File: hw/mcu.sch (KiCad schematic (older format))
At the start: 10 parts, among them U3 MSP430G2553IPW28

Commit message: epd-clock: hw v0.2
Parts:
- added R6, R7: 4.7K, Resistor_SMD:R_0603_1608Metric, symbol Device:R
- renumbered R8 to R5
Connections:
- net +3V3: now also R6.1, R7.1
- net SCL: now also R7.2
- net SDA: now also R6.2
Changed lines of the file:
@@
 $EndDescr
 $Comp
-L power:+3V3 #PWR035
+L power:+3V3 #PWR036
 U 1 1 6113EAC6
 P 5900 2650
-F 0 "#PWR035" H 5900 2500 50  0001 C CNN
+F 0 "#PWR036" H 5900 2500 50  0001 C CNN
 F 1 "+3V3" H 5915 2823 50  0000 C CNN
 F 2 "" H 5900 2650 50  0001 C CNN
@@
 $EndComp
 $Comp
-L power:GND #PWR036
+L power:GND #PWR037
 U 1 1 6113F28C
 P 5900 4850
-F 0 "#PWR036" H 5900 4600 50  0001 C CNN
+F 0 "#PWR037" H 5900 4600 50  0001 C CNN
 F 1 "GND" H 5905 4677 50  0000 C CNN
 F 2 "" H 5900 4850 50  0001 C CNN
@@
 $EndComp
 $Comp
-L Device:R R8
+L Device:R R5
 U 1 1 6113FE92
 P 4150 2650
-F 0 "R8" H 4220 2696 50  0000 L CNN
+F 0 "R5" H 4220 2696 50  0000 L CNN
 F 1 "47K" H 4220 2605 50  0000 L CNN
 F 2 "Resistor_SMD:R_0603_1608Metric" V 4080 2650 50  0001 C CNN
@@
 	4150 2900 4150 3000
 $Comp
-L power:GND #PWR032
+L power:GND #PWR033
 U 1 1 61141837
 P 4150 3300
-F 0 "#PWR032" H 4150 3050 50  0001 C CNN
+F 0 "#PWR033" H 4150 3050 50  0001 C CNN
 F 1 "GND" H 4155 3127 50  0000 C CNN
 F 2 "" H 4150 3300 50  0001 C CNN
@@
 $EndComp
 $Comp
-L power:+3V3 #PWR031
+L power:+3V3 #PWR032
 U 1 1 61141D49
 P 4150 2500
-F 0 "#PWR031" H 4150 2350 50  0001 C CNN
+F 0 "#PWR032" H 4150 2350 50  0001 C CNN
 F 1 "+3V3" H 4165 2673 50  0000 C CNN
 F 2 "" H 4150 2500 50  0001 C CNN
@@
 $EndComp
 $Comp
-L power:+3V3 #PWR033
+L power:+3V3 #PWR034
 U 1 1 611466AB
 P 5150 1750
-F 0 "#PWR033" H 5150 1600 50  0001 C CNN
+F 0 "#PWR034" H 5150 1600 50  0001 C CNN
 F 1 "+3V3" V 5165 1878 50  0000 L CNN
 F 2 "" H 5150 1750 50  0001 C CNN
@@
 $EndComp
 $Comp
-L power:GND #PWR034
+L power:GND #PWR035
 U 1 1 61146C9B
 P 5150 1850
-F 0 "#PWR034" H 5150 1600 50  0001 C CNN
+F 0 "#PWR035" H 5150 1600 50  0001 C CNN
 F 1 "GND" V 5155 1722 50  0000 R CNN
 F 2 "" H 5150 1850 50  0001 C CNN
@@
 Text HLabel 4500 4050 0    50   Output ~ 0
 CLK
-Text HLabel 7300 3650 2    50   Output ~ 0
+Text HLabel 8350 3650 2    50   Output ~ 0
 SCL
-Text HLabel 7300 3750 2    50   BiDi ~ 0
+Text HLabel 8350 3750 2    50   BiDi ~ 0
 SDA
 Text HLabel 4500 4550 0    50   Output ~ 0
@@
 $EndComp
 $Comp
-L power:+3V3 #PWR038
+L power:+3V3 #PWR039
 U 1 1 610AD35D
 P 6450 1900
-F 0 "#PWR038" H 6450 1750 50  0001 C CNN
+F 0 "#PWR039" H 6450 1750 50  0001 C CNN
 F 1 "+3V3" V 6465 2028 50  0000 L CNN
 F 2 "" H 6450 1900 50  0001 C CNN
@@
 $EndComp
 $Comp
-L power:GND #PWR037
+L power:GND #PWR038
 U 1 1 610AD870
 P 6150 1900
-F 0 "#PWR037" H 6150 1650 50  0001 C CNN
+F 0 "#PWR038" H 6150 1650 50  0001 C CNN
 F 1 "GND" V 6155 1772 50  0000 R CNN
 F 2 "" H 6150 1900 50  0001 C CNN
@@
 NoConn ~ 7300 4400
 NoConn ~ 7300 4200
+$Comp
+L Device:R R6
+U 1 1 6117A5A3
+P 8050 3400
+F 0 "R6" H 8120 3446 50  0000 L CNN
+F 1 "4.7K" H 8120 3355 50  0000 L CNN
+F 2 "Resistor_SMD:R_0603_1608Metric" V 7980 3400 50  0001 C CNN
+F 3 "~" H 8050 3400 50  0001 C CNN
+	1    8050 3400
+	1    0    0    -1
+$EndComp
+$Comp
+L Device:R R7
+U 1 1 6117B220
+P 8300 3400
+F 0 "R7" H 8370 3446 50  0000 L CNN
+F 1 "4.7K" H 8370 3355 50  0000 L CNN
+F 2 "Resistor_SMD:R_0603_1608Metric" V 8230 3400 50  0001 C CNN
+F 3 "~" H 8300 3400 50  0001 C CNN
+	1    8300 3400
+	1    0    0    -1
+$EndComp
+Wire Wire Line
+	7300 3750 8050 3750
+Wire Wire Line
+	8350 3650 8300 3650
+Wire Wire Line
+	8050 3550 8050 3750
+Connection ~ 8050 3750
+Wire Wire Line
+	8050 3750 8350 3750
+Wire Wire Line
+	8300 3550 8300 3650
+Connection ~ 8300 3650
+Wire Wire Line
+	8300 3650 7300 3650
+$Comp
+L power:+3V3 #PWR040
+U 1 1 6117E515
+P 8050 3250
+F 0 "#PWR040" H 8050 3100 50  0001 C CNN
+F 1 "+3V3" H 8065 3423 50  0000 C CNN
+F 2 "" H 8050 3250 50  0001 C CNN
+F 3 "" H 8050 3250 50  0001 C CNN
+	1    8050 3250
+	1    0    0    -1
+$EndComp
+$Comp
+L power:+3V3 #PWR041
+U 1 1 6117EB1C
+P 8300 3250
+F 0 "#PWR041" H 8300 3100 50  0001 C CNN
+F 1 "+3V3" H 8315 3423 50  0000 C CNN
+F 2 "" H 8300 3250 50  0001 C CNN
+F 3 "" H 8300 3250 50  0001 C CNN
+	1    8300 3250
+	1    0    0    -1
+$EndComp
 $EndSCHEMATC

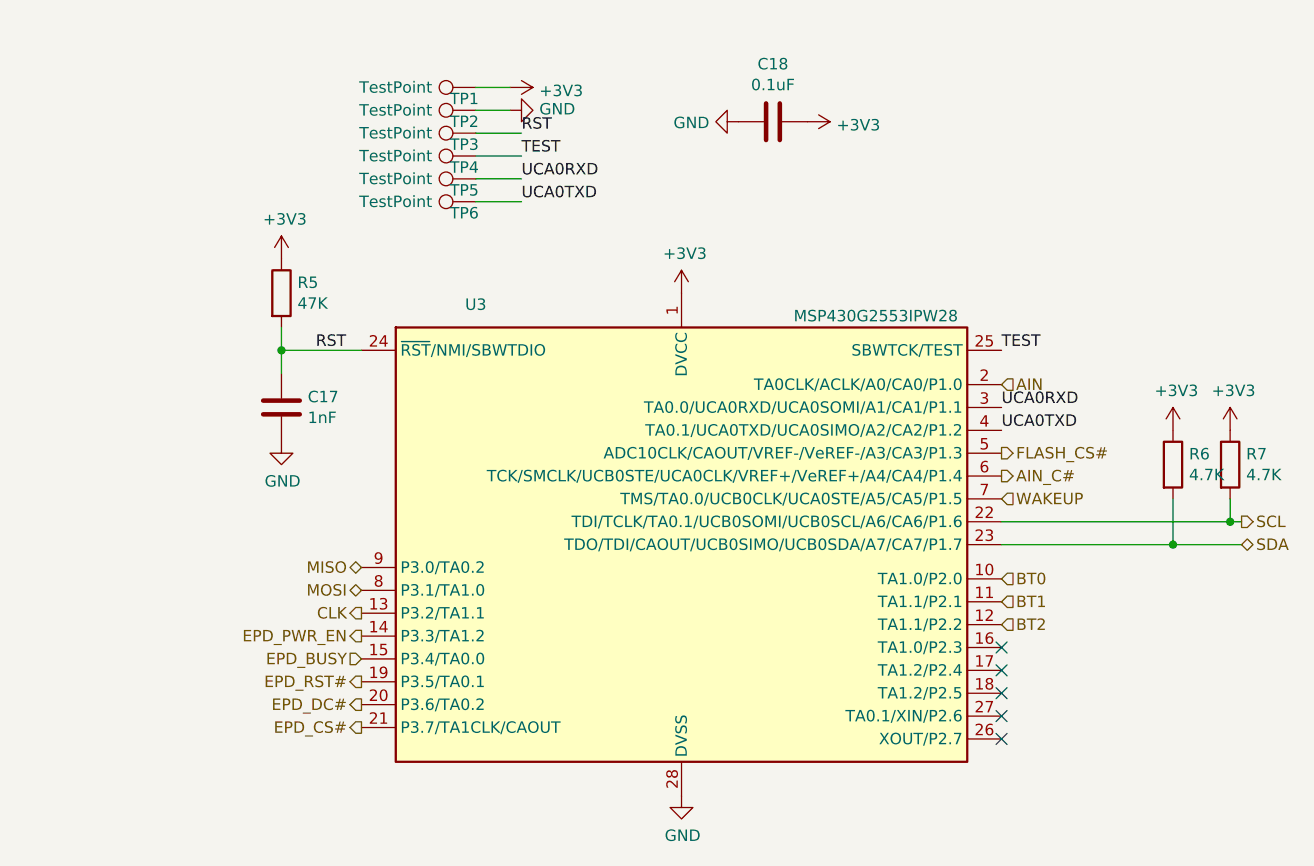
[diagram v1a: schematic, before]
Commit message: epd-clock hw: add i2c test point
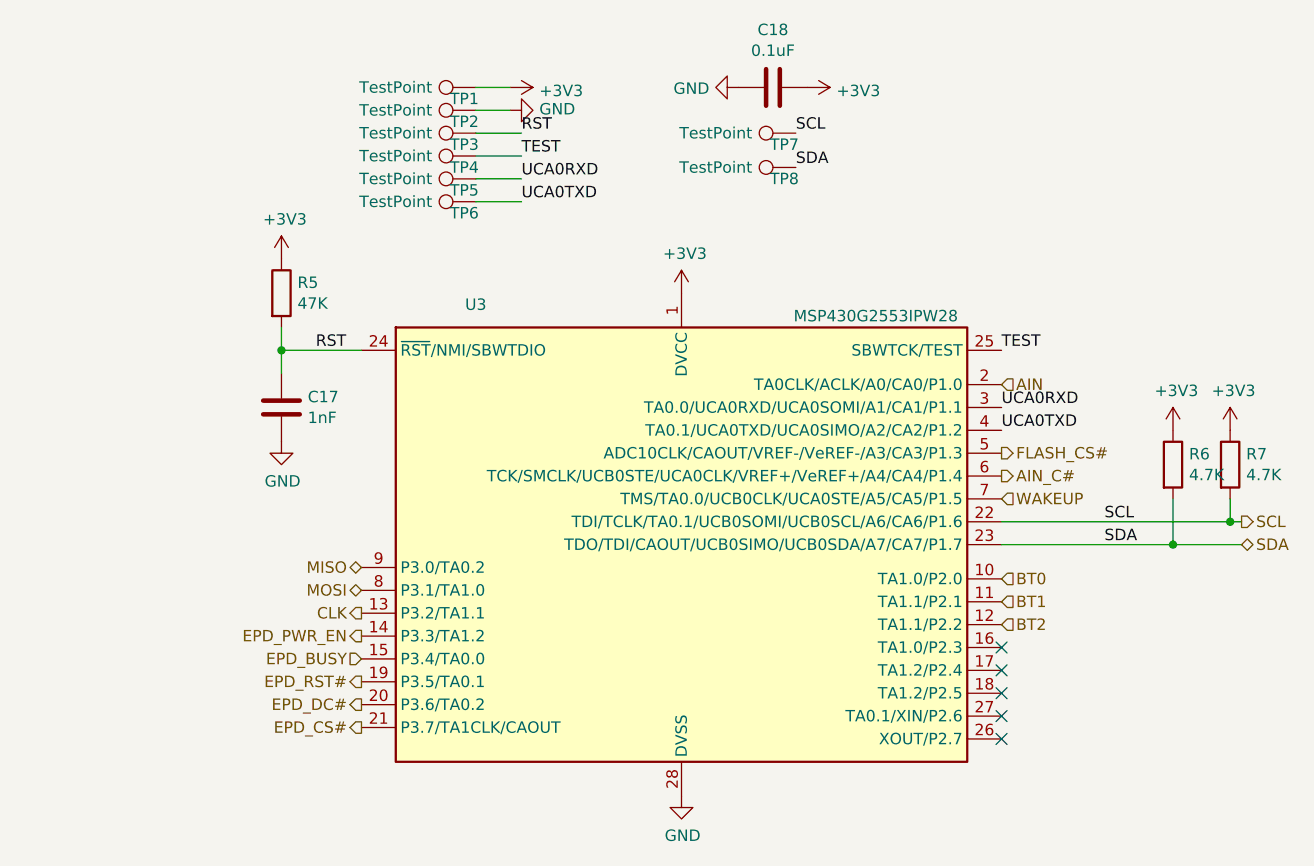
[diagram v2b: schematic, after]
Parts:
- added TP7, TP8: TestPoint, TestPoint:TestPoint_Pad_D1.0mm, symbol Connector:TestPoint
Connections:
- net SCL: now also TP7.1
- net SDA: now also TP8.1
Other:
- moved on the sheet: C18
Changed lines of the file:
@@
 L Device:C C18
 U 1 1 610AA82E
-P 6300 1900
-F 0 "C18" V 6048 1900 50  0000 C CNN
-F 1 "0.1uF" V 6139 1900 50  0000 C CNN
-F 2 "Capacitor_SMD:C_0603_1608Metric" H 6338 1750 50  0001 C CNN
-F 3 "~" H 6300 1900 50  0001 C CNN
-	1    6300 1900
+P 6300 1750
+F 0 "C18" V 6048 1750 50  0000 C CNN
+F 1 "0.1uF" V 6139 1750 50  0000 C CNN
+F 2 "Capacitor_SMD:C_0603_1608Metric" H 6338 1600 50  0001 C CNN
+F 3 "~" H 6300 1750 50  0001 C CNN
+	1    6300 1750
 	0    1    1    0
 $EndComp
@@
 L power:+3V3 #PWR039
 U 1 1 610AD35D
-P 6450 1900
-F 0 "#PWR039" H 6450 1750 50  0001 C CNN
-F 1 "+3V3" V 6465 2028 50  0000 L CNN
-F 2 "" H 6450 1900 50  0001 C CNN
-F 3 "" H 6450 1900 50  0001 C CNN
-	1    6450 1900
+P 6450 1750
+F 0 "#PWR039" H 6450 1600 50  0001 C CNN
+F 1 "+3V3" V 6465 1878 50  0000 L CNN
+F 2 "" H 6450 1750 50  0001 C CNN
+F 3 "" H 6450 1750 50  0001 C CNN
+	1    6450 1750
 	0    1    1    0
 $EndComp
@@
 L power:GND #PWR038
 U 1 1 610AD870
-P 6150 1900
-F 0 "#PWR038" H 6150 1650 50  0001 C CNN
-F 1 "GND" V 6155 1772 50  0000 R CNN
-F 2 "" H 6150 1900 50  0001 C CNN
-F 3 "" H 6150 1900 50  0001 C CNN
-	1    6150 1900
+P 6150 1750
+F 0 "#PWR038" H 6150 1500 50  0001 C CNN
+F 1 "GND" V 6155 1622 50  0000 R CNN
+F 2 "" H 6150 1750 50  0001 C CNN
+F 3 "" H 6150 1750 50  0001 C CNN
+	1    6150 1750
 	0    1    1    0
 $EndComp
@@
 	1    0    0    -1
 $EndComp
+$Comp
+L Connector:TestPoint TP7
+U 1 1 6117E188
+P 6400 1950
+F 0 "TP7" V 6350 2000 50  0000 C CNN
+F 1 "TestPoint" V 6400 2300 50  0000 C CNN
+F 2 "TestPoint:TestPoint_Pad_D1.0mm" H 6600 1950 50  0001 C CNN
+F 3 "~" H 6600 1950 50  0001 C CNN
+	1    6400 1950
+	0    -1   -1   0
+$EndComp
+$Comp
+L Connector:TestPoint TP8
+U 1 1 61186342
+P 6400 2100
+F 0 "TP8" V 6350 2150 50  0000 C CNN
+F 1 "TestPoint" V 6400 2450 50  0000 C CNN
+F 2 "TestPoint:TestPoint_Pad_D1.0mm" H 6600 2100 50  0001 C CNN
+F 3 "~" H 6600 2100 50  0001 C CNN
+	1    6400 2100
+	0    -1   -1   0
+$EndComp
+Text Label 7750 3650 0    50   ~ 0
+SCL
+Text Label 7750 3750 0    50   ~ 0
+SDA
+Text Label 6400 2100 0    50   ~ 0
+SDA
+Text Label 6400 1950 0    50   ~ 0
+SCL
 $EndSCHEMATC

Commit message: epd-clock: hw: v0.2
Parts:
- added R7, R8, R9: 10K, Resistor_SMD:R_0603_1608Metric, symbol Device:R
- renumbered C17 to C16, C18 to C17, R5 to R10, R6 to R11, R7 to R12, U3 to U2
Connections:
- net +3V3: now also R7.1, R8.1, R9.1
- net CLK: now also R7.2
- net EPD_BUSY: now also U2.8 (P3.1/TA1.0); no longer U2.15 (P3.4/TA0.0)
- net EPD_CS#: now also U2.19 (P3.5/TA0.1); no longer U2.21 (P3.7/TA1CLK/CAOUT)
- net EPD_RST#: now also U2.21 (P3.7/TA1CLK/CAOUT); no longer U2.19 (P3.5/TA0.1)
- net MISO: now also R9.2
- net MOSI: now also U2.15 (P3.4/TA0.0), R8.2; no longer U2.8 (P3.1/TA1.0)
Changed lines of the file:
@@
 $EndDescr
 $Comp
-L power:+3V3 #PWR036
+L power:+3V3 #PWR034
 U 1 1 6113EAC6
 P 5900 2650
-F 0 "#PWR036" H 5900 2500 50  0001 C CNN
+F 0 "#PWR034" H 5900 2500 50  0001 C CNN
 F 1 "+3V3" H 5915 2823 50  0000 C CNN
 F 2 "" H 5900 2650 50  0001 C CNN
@@
 $EndComp
 $Comp
-L power:GND #PWR037
+L power:GND #PWR035
 U 1 1 6113F28C
 P 5900 4850
-F 0 "#PWR037" H 5900 4600 50  0001 C CNN
+F 0 "#PWR035" H 5900 4600 50  0001 C CNN
 F 1 "GND" H 5905 4677 50  0000 C CNN
 F 2 "" H 5900 4850 50  0001 C CNN
@@
 $EndComp
 $Comp
-L Device:R R5
+L Device:R R10
 U 1 1 6113FE92
 P 4150 2650
-F 0 "R5" H 4220 2696 50  0000 L CNN
+F 0 "R10" H 4220 2696 50  0000 L CNN
 F 1 "47K" H 4220 2605 50  0000 L CNN
 F 2 "Resistor_SMD:R_0603_1608Metric" V 4080 2650 50  0001 C CNN
@@
 $EndComp
 $Comp
-L Device:C C17
+L Device:C C16
 U 1 1 61140B33
 P 4150 3150
-F 0 "C17" H 4265 3196 50  0000 L CNN
+F 0 "C16" H 4265 3196 50  0000 L CNN
 F 1 "1nF" H 4265 3105 50  0000 L CNN
 F 2 "Capacitor_SMD:C_0603_1608Metric" H 4188 3000 50  0001 C CNN
@@
 	4150 2900 4150 3000
 $Comp
-L power:GND #PWR033
+L power:GND #PWR031
 U 1 1 61141837
 P 4150 3300
-F 0 "#PWR033" H 4150 3050 50  0001 C CNN
+F 0 "#PWR031" H 4150 3050 50  0001 C CNN
 F 1 "GND" H 4155 3127 50  0000 C CNN
 F 2 "" H 4150 3300 50  0001 C CNN
@@
 $EndComp
 $Comp
-L power:+3V3 #PWR032
+L power:+3V3 #PWR030
 U 1 1 61141D49
 P 4150 2500
-F 0 "#PWR032" H 4150 2350 50  0001 C CNN
+F 0 "#PWR030" H 4150 2350 50  0001 C CNN
 F 1 "+3V3" H 4165 2673 50  0000 C CNN
 F 2 "" H 4150 2500 50  0001 C CNN
@@
 $EndComp
 $Comp
-L power:+3V3 #PWR034
+L power:+3V3 #PWR032
 U 1 1 611466AB
 P 5150 1750
-F 0 "#PWR034" H 5150 1600 50  0001 C CNN
+F 0 "#PWR032" H 5150 1600 50  0001 C CNN
 F 1 "+3V3" V 5165 1878 50  0000 L CNN
 F 2 "" H 5150 1750 50  0001 C CNN
@@
 $EndComp
 $Comp
-L power:GND #PWR035
+L power:GND #PWR033
 U 1 1 61146C9B
 P 5150 1850
-F 0 "#PWR035" H 5150 1600 50  0001 C CNN
+F 0 "#PWR033" H 5150 1600 50  0001 C CNN
 F 1 "GND" V 5155 1722 50  0000 R CNN
 F 2 "" H 5150 1850 50  0001 C CNN
@@
 Text HLabel 4500 3850 0    50   BiDi ~ 0
 MISO
-Text HLabel 4500 3950 0    50   BiDi ~ 0
+Text HLabel 4500 4250 0    50   BiDi ~ 0
 MOSI
-Text HLabel 4500 4050 0    50   Output ~ 0
-CLK
 Text HLabel 8350 3650 2    50   Output ~ 0
 SCL
 Text HLabel 8350 3750 2    50   BiDi ~ 0
 SDA
-Text HLabel 4500 4550 0    50   Output ~ 0
+Text HLabel 4500 4350 0    50   Output ~ 0
 EPD_CS#
 Text HLabel 7300 3350 2    50   Output ~ 0
@@
 Text HLabel 4500 4150 0    50   Output ~ 0
 EPD_PWR_EN
-Text HLabel 4500 4250 0    50   Input ~ 0
+Text HLabel 4500 3950 0    50   Input ~ 0
 EPD_BUSY
-Text HLabel 4500 4350 0    50   Output ~ 0
-EPD_RST#
 Text HLabel 4500 4450 0    50   Output ~ 0
 EPD_DC#
@@
 NoConn ~ 7300 4500
 $Comp
-L Device:C C18
+L Device:C C17
 U 1 1 610AA82E
 P 6300 1750
-F 0 "C18" V 6048 1750 50  0000 C CNN
+F 0 "C17" V 6048 1750 50  0000 C CNN
 F 1 "0.1uF" V 6139 1750 50  0000 C CNN
 F 2 "Capacitor_SMD:C_0603_1608Metric" H 6338 1600 50  0001 C CNN
@@
 $EndComp
 $Comp
-L power:+3V3 #PWR039
+L power:+3V3 #PWR037
 U 1 1 610AD35D
 P 6450 1750
-F 0 "#PWR039" H 6450 1600 50  0001 C CNN
+F 0 "#PWR037" H 6450 1600 50  0001 C CNN
 F 1 "+3V3" V 6465 1878 50  0000 L CNN
 F 2 "" H 6450 1750 50  0001 C CNN
@@
 $EndComp
 $Comp
-L power:GND #PWR038
+L power:GND #PWR036
 U 1 1 610AD870
 P 6150 1750
-F 0 "#PWR038" H 6150 1500 50  0001 C CNN
+F 0 "#PWR036" H 6150 1500 50  0001 C CNN
 F 1 "GND" V 6155 1622 50  0000 R CNN
 F 2 "" H 6150 1750 50  0001 C CNN
@@
 	5000 2250 5200 2250
 $Comp
-L MCU_Texas_MSP430:MSP430G2553IPW28 U3
+L MCU_Texas_MSP430:MSP430G2553IPW28 U2
 U 1 1 6113C1EF
 P 5900 3750
-F 0 "U3" H 5000 4800 50  0000 C CNN
+F 0 "U2" H 5000 4800 50  0000 C CNN
 F 1 "MSP430G2553IPW28" H 6750 4750 50  0000 C CNN
 F 2 "Package_SO:TSSOP-28_4.4x9.7mm_P0.65mm" H 4750 2750 50  0001 C CIN
@@
 NoConn ~ 7300 4200
 $Comp
-L Device:R R6
+L Device:R R11
 U 1 1 6117A5A3
 P 8050 3400
-F 0 "R6" H 8120 3446 50  0000 L CNN
+F 0 "R11" H 8120 3446 50  0000 L CNN
 F 1 "4.7K" H 8120 3355 50  0000 L CNN
 F 2 "Resistor_SMD:R_0603_1608Metric" V 7980 3400 50  0001 C CNN
@@
 $EndComp
 $Comp
-L Device:R R7
+L Device:R R12
 U 1 1 6117B220
 P 8300 3400
-F 0 "R7" H 8370 3446 50  0000 L CNN
+F 0 "R12" H 8370 3446 50  0000 L CNN
 F 1 "4.7K" H 8370 3355 50  0000 L CNN
 F 2 "Resistor_SMD:R_0603_1608Metric" V 8230 3400 50  0001 C CNN
@@
 	8300 3650 7300 3650
 $Comp
-L power:+3V3 #PWR040
+L power:+3V3 #PWR038
 U 1 1 6117E515
 P 8050 3250
-F 0 "#PWR040" H 8050 3100 50  0001 C CNN
+F 0 "#PWR038" H 8050 3100 50  0001 C CNN
 F 1 "+3V3" H 8065 3423 50  0000 C CNN
 F 2 "" H 8050 3250 50  0001 C CNN
@@
 $EndComp
 $Comp
-L power:+3V3 #PWR041
+L power:+3V3 #PWR039
 U 1 1 6117EB1C
 P 8300 3250
-F 0 "#PWR041" H 8300 3100 50  0001 C CNN
+F 0 "#PWR039" H 8300 3100 50  0001 C CNN
 F 1 "+3V3" H 8315 3423 50  0000 C CNN
 F 2 "" H 8300 3250 50  0001 C CNN
@@
 Text Label 6400 1950 0    50   ~ 0
 SCL
+$Comp
+L Device:R R9
+U 1 1 611AD488
+P 3700 3500
+F 0 "R9" H 3770 3546 50  0000 L CNN
+F 1 "10K" H 3770 3455 50  0000 L CNN
+F 2 "Resistor_SMD:R_0603_1608Metric" V 3630 3500 50  0001 C CNN
+F 3 "~" H 3700 3500 50  0001 C CNN
+	1    3700 3500
+	1    0    0    -1
+$EndComp
+$Comp
+L Device:R R8
+U 1 1 611B1822
+P 3400 3500
+F 0 "R8" H 3470 3546 50  0000 L CNN
+F 1 "10K" H 3470 3455 50  0000 L CNN
+F 2 "Resistor_SMD:R_0603_1608Metric" V 3330 3500 50  0001 C CNN
+F 3 "~" H 3400 3500 50  0001 C CNN
+	1    3400 3500
+	1    0    0    -1
+$EndComp
+$Comp
+L Device:R R7
+U 1 1 611B1D89
+P 3100 3500
+F 0 "R7" H 3170 3546 50  0000 L CNN
+F 1 "10K" H 3170 3455 50  0000 L CNN
+F 2 "Resistor_SMD:R_0603_1608Metric" V 3030 3500 50  0001 C CNN
+F 3 "~" H 3100 3500 50  0001 C CNN
+	1    3100 3500
+	1    0    0    -1
+$EndComp
+$Comp
+L power:+3V3 #PWR027
+U 1 1 611B222A
+P 3100 3350
+F 0 "#PWR027" H 3100 3200 50  0001 C CNN
+F 1 "+3V3" H 3115 3523 50  0000 C CNN
+F 2 "" H 3100 3350 50  0001 C CNN
+F 3 "" H 3100 3350 50  0001 C CNN
+	1    3100 3350
+	1    0    0    -1
+$EndComp
+$Comp
+L power:+3V3 #PWR028
+U 1 1 611B294F
+P 3400 3350
+F 0 "#PWR028" H 3400 3200 50  0001 C CNN
+F 1 "+3V3" H 3415 3523 50  0000 C CNN
+F 2 "" H 3400 3350 50  0001 C CNN
+F 3 "" H 3400 3350 50  0001 C CNN
+	1    3400 3350
+	1    0    0    -1
+$EndComp
+$Comp
+L power:+3V3 #PWR029
+U 1 1 611B2EF1
+P 3700 3350
+F 0 "#PWR029" H 3700 3200 50  0001 C CNN
+F 1 "+3V3" H 3715 3523 50  0000 C CNN
+F 2 "" H 3700 3350 50  0001 C CNN
+F 3 "" H 3700 3350 50  0001 C CNN
+	1    3700 3350
+	1    0    0    -1
+$EndComp
+Wire Wire Line
+	4500 3850 3700 3850
+Wire Wire Line
+	3700 3850 3700 3650
+Wire Wire Line
+	4500 4050 3100 4050
+Wire Wire Line
+	3100 4050 3100 3650
+Text HLabel 4500 4550 0    50   Output ~ 0
+EPD_RST#
+Text HLabel 4500 4050 0    50   Output ~ 0
+CLK
+Wire Wire Line
+	3400 4250 4500 4250
+Wire Wire Line
+	3400 3650 3400 4250
 $EndSCHEMATC
